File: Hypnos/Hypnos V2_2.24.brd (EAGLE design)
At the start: 25.6 x 52 mm, 32 parts

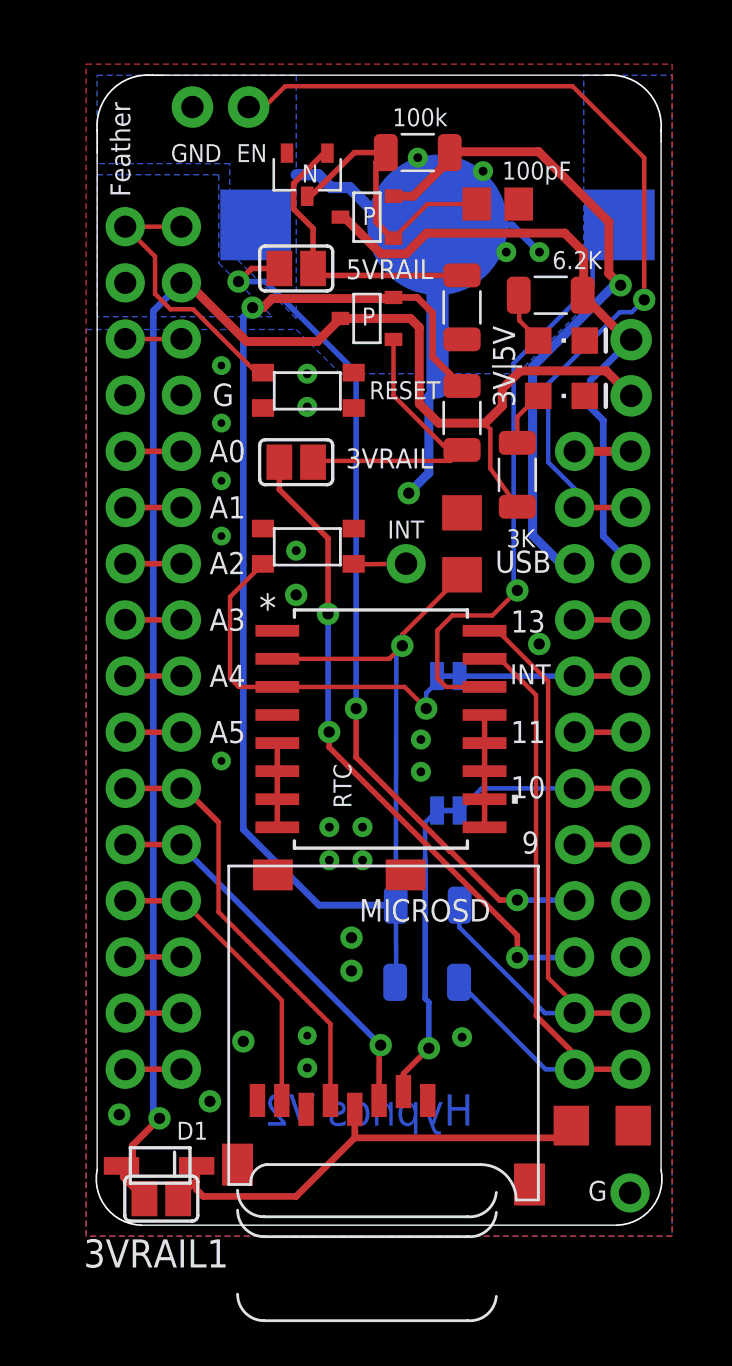
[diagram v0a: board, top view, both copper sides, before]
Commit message: I2C line connected to 3.3Rail
Remoce I2C line from 3.3Rail reduce power going back to sersor when they are turned off.
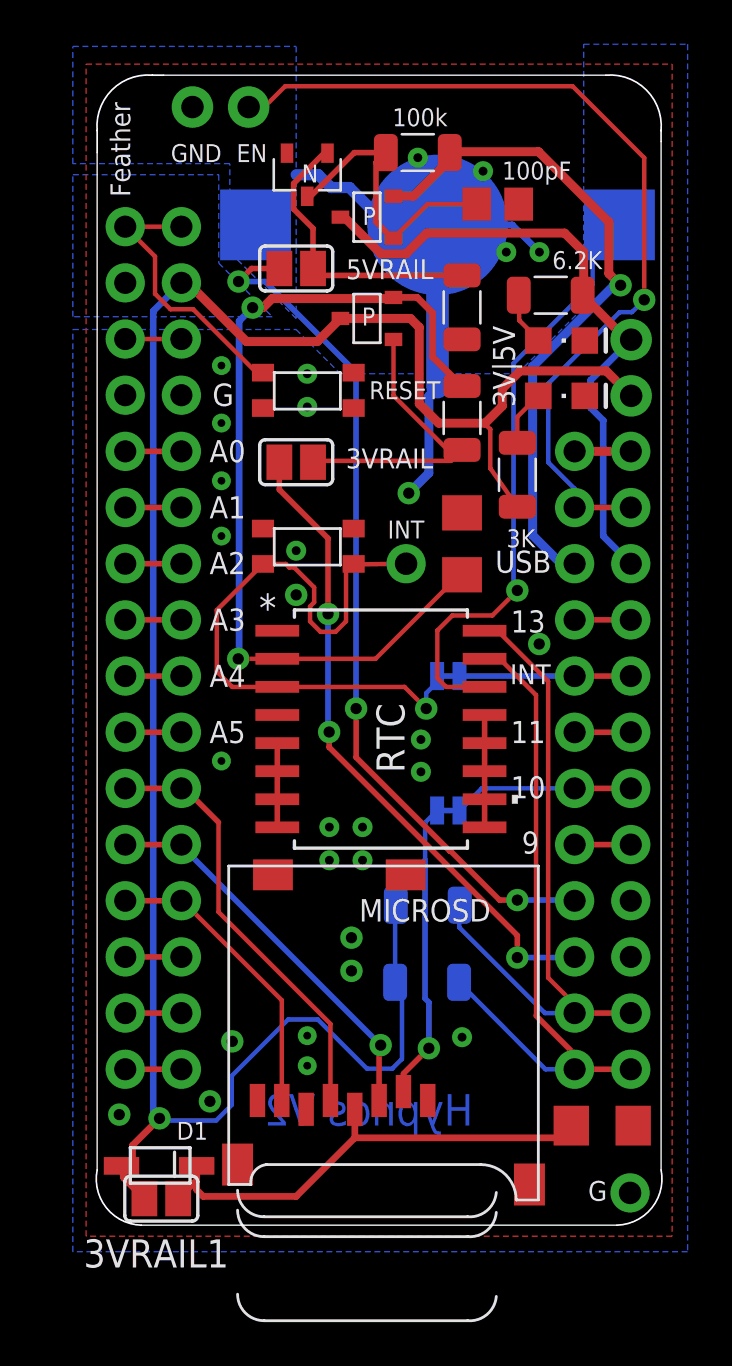
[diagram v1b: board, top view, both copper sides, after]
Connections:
- net +3V3: no longer R6.1, R7.1
- net 3VRAIL: now also R6.1, R7.1
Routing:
- net +3V3: track 70.2 -> 40.3 mm
- net 3VRAIL: track 75.3 -> 97.2 mm
- net RTC_INT: track 19.3 -> 29.1 mm
